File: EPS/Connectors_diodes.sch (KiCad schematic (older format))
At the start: 20 parts

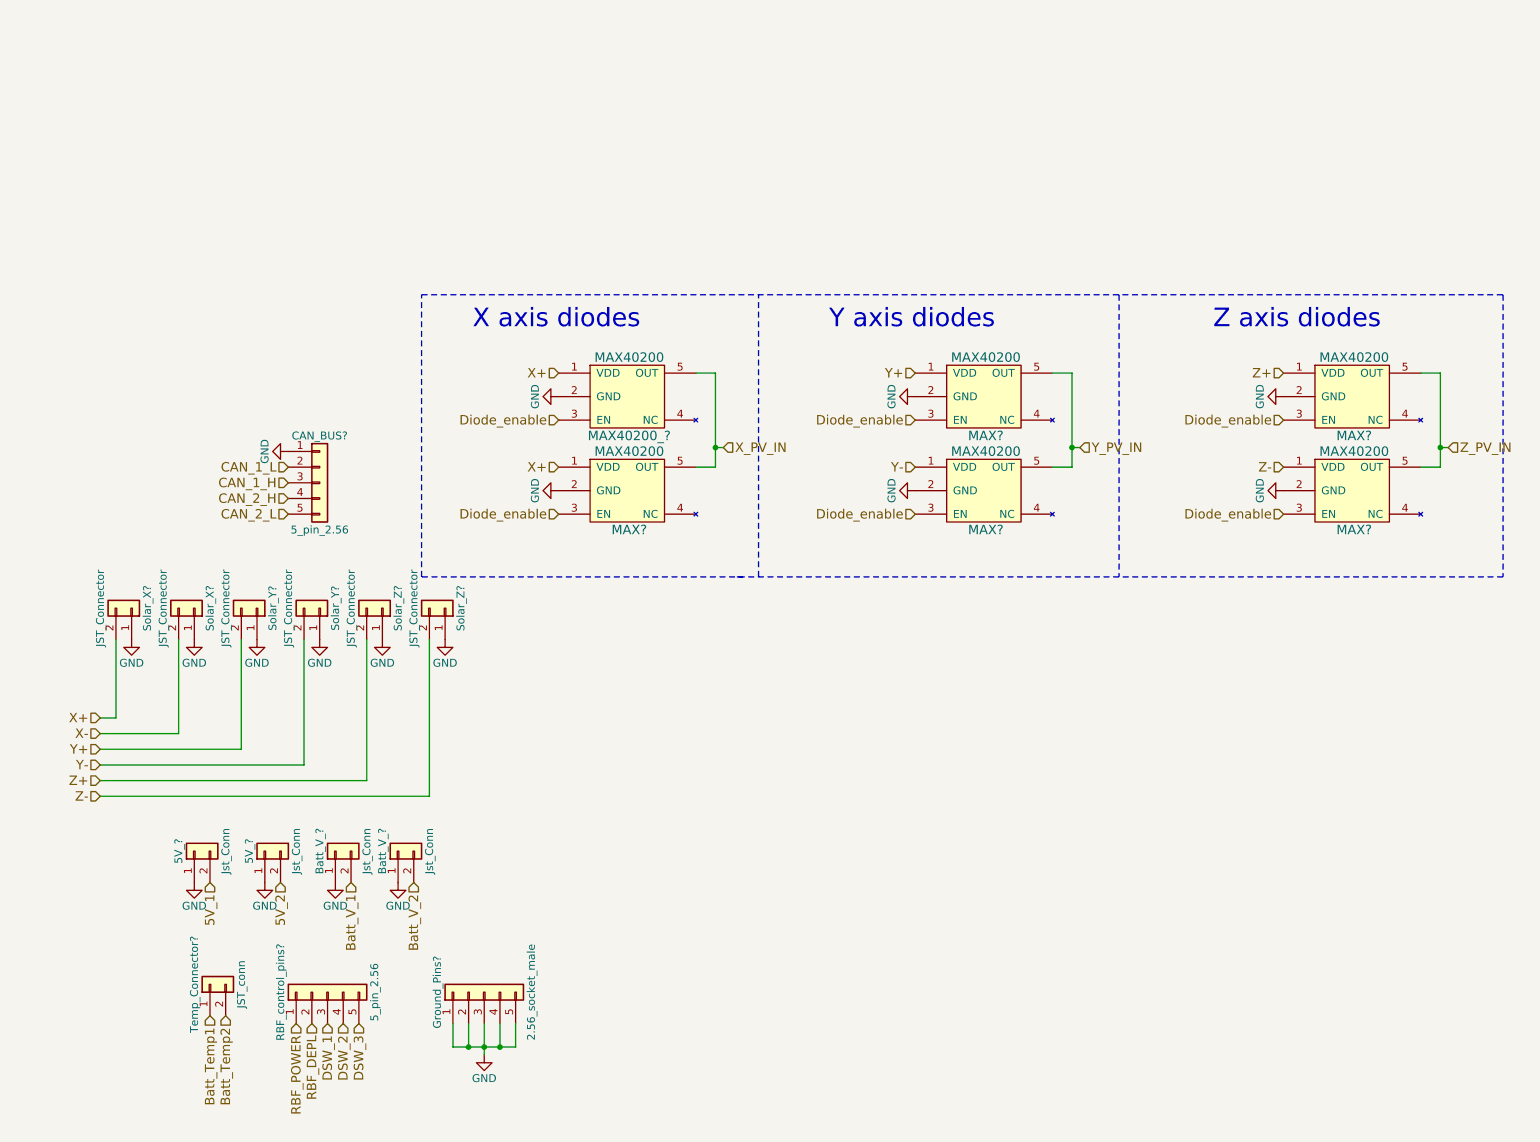
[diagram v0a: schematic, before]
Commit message: Finalized SCH (beta version) and started pcb
Capacitor banks might need to be reassigned to other locations.
No RBF pin on this SCH or PCB.
Battery gound deployment switch is fully mechanical (no mosfet switch on low side).
PCB of the prototype started. Main power converters and current measuring devices layed out.
SCH still requires ESD protection diodes!
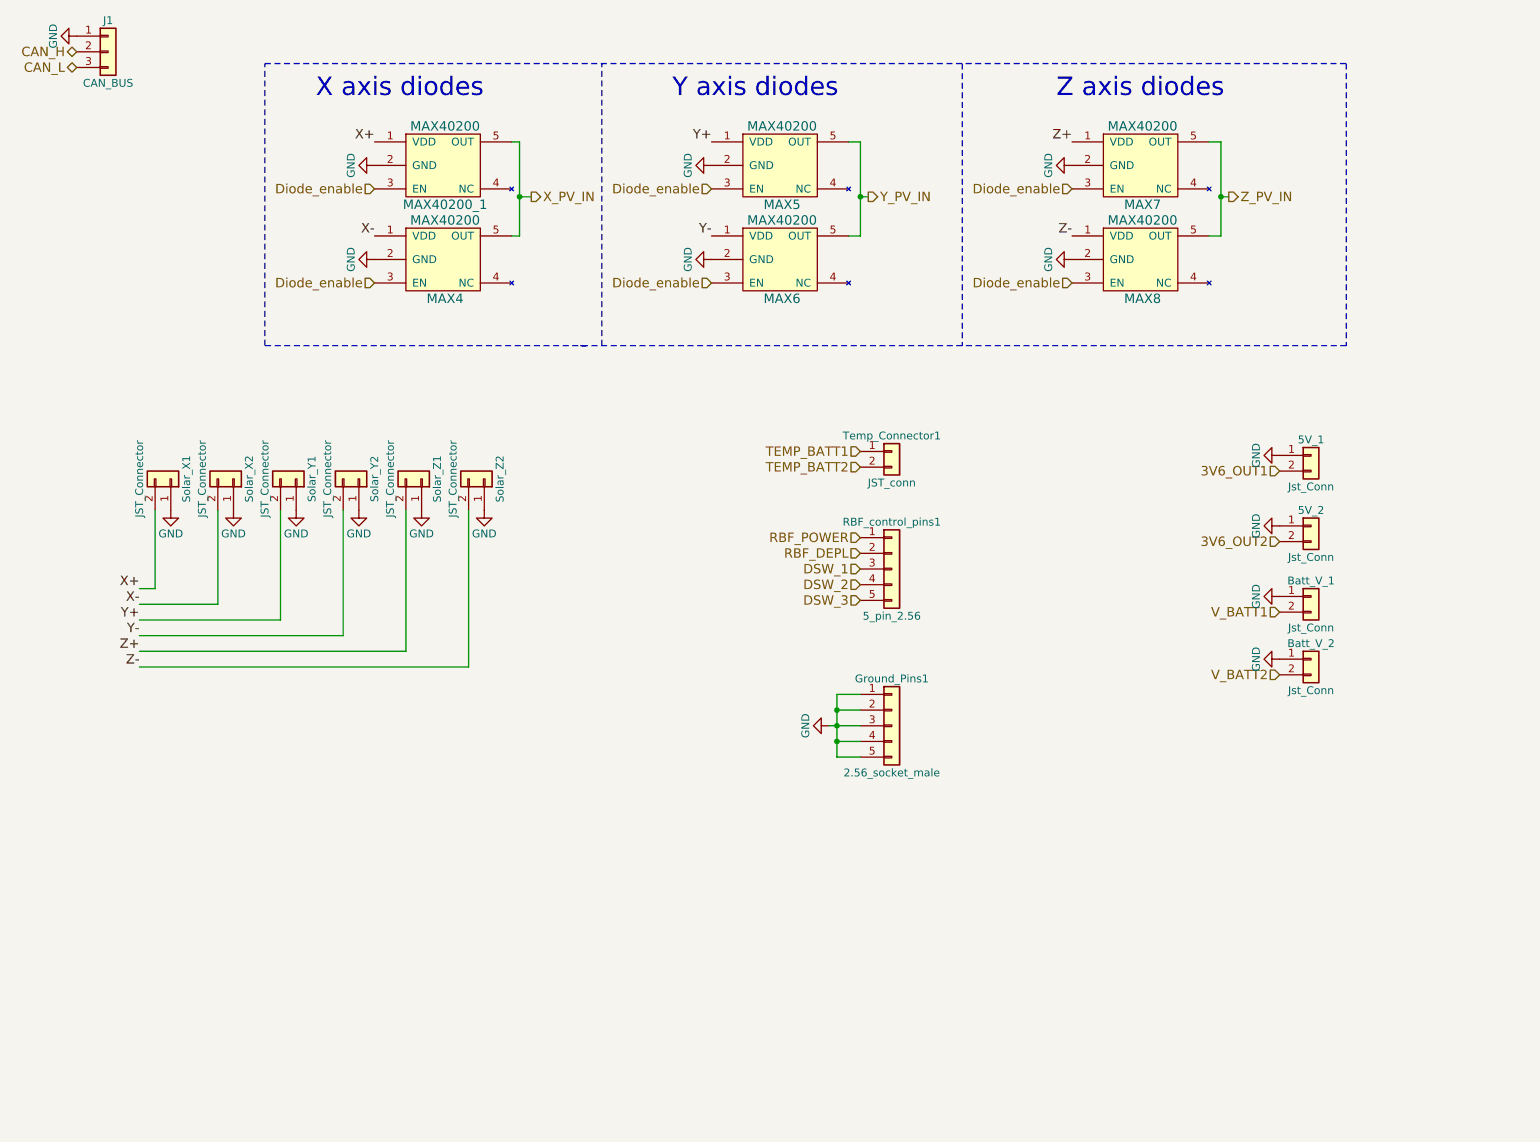
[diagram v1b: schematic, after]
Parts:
- removed CAN_BUS?: 5_pin_2.56, Socket_Strips:Socket_Strip_Straight_1x05_Pitch2.54mm, symbol Conn_01x05
- added J1: CAN_BUS, Housings_SOIC:SOIC-8_3.9x4.9mm_Pitch1.27mm, symbol Conn_01x03
- MAX4, MAX5, MAX6, MAX7, MAX8: renamed from MAX?; footprint (none) -> TO_SOT_Packages_SMD:SOT-23-5
- MAX40200_1: renamed from MAX40200_?; footprint (none) -> TO_SOT_Packages_SMD:SOT-23-5
- gave numbers to parts that had none: 13
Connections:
- net GND: now also J1.1 (Pin_1)
- net X+: no longer MAX4.1 (VDD)
- net X-: now also MAX4.1 (VDD)
- net 5V_1 renamed 3V6_OUT1
- net 5V_2 renamed 3V6_OUT2
- net Batt_Temp1 renamed TEMP_BATT1
- net Batt_Temp2 renamed TEMP_BATT2
- net Batt_V_1 renamed V_BATT1
- net Batt_V_2 renamed V_BATT2
- new net CAN_H: J1.2 (Pin_2)
- new net CAN_L: J1.3 (Pin_3)
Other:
- moved on the sheet: 5V_1, 5V_2, Batt_V_1, Batt_V_2, Ground_Pins1, MAX4, MAX40200_1, MAX5, MAX6, MAX7, MAX8, RBF_control_pins1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

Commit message: PCB updated
Added testpoints and updated PCB
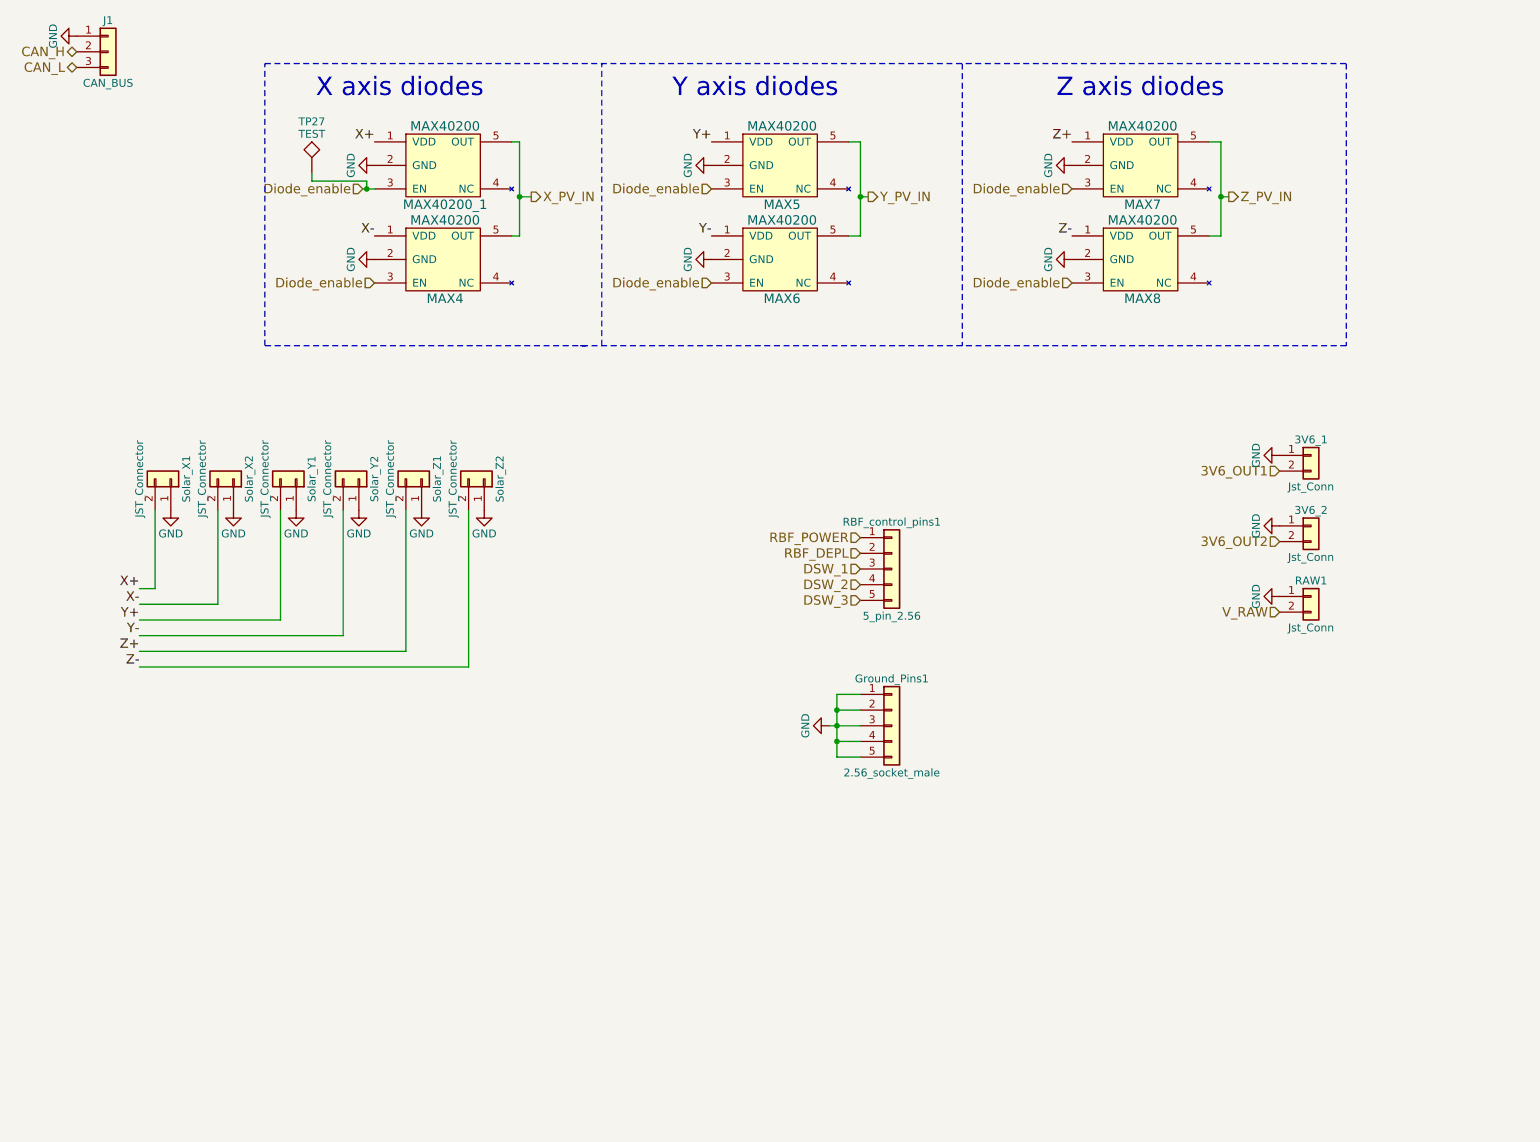
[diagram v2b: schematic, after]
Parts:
- removed Batt_V_2: Jst_Conn, Connectors_JST:JST_XH_B02B-XH-A_02x2.50mm_Straight, symbol Conn_01x02
- removed Temp_Connector1: JST_conn, Connectors_JST:JST_XH_B02B-XH-A_02x2.50mm_Straight, symbol Conn_01x02
- added TP27: TEST, Measurement_Points:Measurement_Point_Round-SMD-Pad_Small, symbol TEST
- J1: footprint Housings_SOIC:SOIC-8_3.9x4.9mm_Pitch1.27mm -> Pin_Headers:Pin_Header_Straight_1x03_Pitch2.54mm
- renumbered 5V_1 to 3V6_1, 5V_2 to 3V6_2, Batt_V_1 to RAW1
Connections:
- net Diode_enable: now also TP27.1
- net V_BATT1 renamed V_RAW
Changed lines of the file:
@@
 $EndComp
 $Comp
-L GND #PWR0135
+L GND #PWR0134
 U 1 1 5A8B7527
 P 3300 1825
-F 0 "#PWR0135" H 3300 1575 50  0001 C CNN
+F 0 "#PWR0134" H 3300 1575 50  0001 C CNN
 F 1 "GND" H 3300 1675 50  0000 C CNN
 F 2 "" H 3300 1825 50  0001 C CNN
@@
 $EndComp
 $Comp
-L GND #PWR0136
+L GND #PWR0135
 U 1 1 5A8B755E
 P 3300 2425
-F 0 "#PWR0136" H 3300 2175 50  0001 C CNN
+F 0 "#PWR0135" H 3300 2175 50  0001 C CNN
 F 1 "GND" H 3300 2275 50  0000 C CNN
 F 2 "" H 3300 2425 50  0001 C CNN
@@
 $EndComp
 $Comp
-L GND #PWR0137
+L GND #PWR0136
 U 1 1 5A8B757B
 P 5450 1825
-F 0 "#PWR0137" H 5450 1575 50  0001 C CNN
+F 0 "#PWR0136" H 5450 1575 50  0001 C CNN
 F 1 "GND" H 5450 1675 50  0000 C CNN
 F 2 "" H 5450 1825 50  0001 C CNN
@@
 $EndComp
 $Comp
-L GND #PWR0138
+L GND #PWR0137
 U 1 1 5A8B7598
 P 5450 2425
-F 0 "#PWR0138" H 5450 2175 50  0001 C CNN
+F 0 "#PWR0137" H 5450 2175 50  0001 C CNN
 F 1 "GND" H 5450 2275 50  0000 C CNN
 F 2 "" H 5450 2425 50  0001 C CNN
@@
 $EndComp
 $Comp
-L GND #PWR0139
+L GND #PWR0138
 U 1 1 5A8B75B5
 P 7750 1825
-F 0 "#PWR0139" H 7750 1575 50  0001 C CNN
+F 0 "#PWR0138" H 7750 1575 50  0001 C CNN
 F 1 "GND" H 7750 1675 50  0000 C CNN
 F 2 "" H 7750 1825 50  0001 C CNN
@@
 $EndComp
 $Comp
-L GND #PWR0140
+L GND #PWR0139
 U 1 1 5A8B75D2
 P 7750 2425
-F 0 "#PWR0140" H 7750 2175 50  0001 C CNN
+F 0 "#PWR0139" H 7750 2175 50  0001 C CNN
 F 1 "GND" H 7750 2275 50  0000 C CNN
 F 2 "" H 7750 2425 50  0001 C CNN
@@
 3V6_OUT2
 Text HLabel 9075 4675 0    60   Input ~ 0
-V_BATT1
-Text HLabel 9075 5075 0    60   Input ~ 0
-V_BATT2
+V_RAW
 Text HLabel 6400 4300 0    60   Input ~ 0
 RBF_DEPL
@@
 Wire Wire Line
 	1800 5025 3900 5025
-Text HLabel 6400 3650 0    60   Input ~ 0
-TEMP_BATT1
-Text HLabel 6400 3750 0    60   Input ~ 0
-TEMP_BATT2
 $Comp
 L Conn_01x02 Solar_X1
@@
 $EndComp
 $Comp
-L Conn_01x02 5V_2
+L Conn_01x02 3V6_2
 U 1 1 5A8D8080
 P 9275 4125
-F 0 "5V_2" H 9275 4225 50  0000 C CNN
+F 0 "3V6_2" H 9275 4225 50  0000 C CNN
 F 1 "Jst_Conn" H 9275 3925 50  0000 C CNN
 F 2 "Connectors_JST:JST_XH_B02B-XH-A_02x2.50mm_Straight" H 9275 4125 50  0001 C CNN
 F 3 "" H 9275 4125 50  0001 C CNN
 	1    9275 4125
-	1    0    0    -1
-$EndComp
-$Comp
-L Conn_01x02 Temp_Connector1
-U 1 1 5A8D8081
-P 6600 3650
-F 0 "Temp_Connector1" H 6600 3750 50  0000 C CNN
-F 1 "JST_conn" H 6600 3450 50  0000 C CNN
-F 2 "Connectors_JST:JST_XH_B02B-XH-A_02x2.50mm_Straight" H 6600 3650 50  0001 C CNN
-F 3 "" H 6600 3650 50  0001 C CNN
-	1    6600 3650
 	1    0    0    -1
 $EndComp
@@
 $EndComp
 $Comp
-L Conn_01x02 Batt_V_2
-U 1 1 5A8D8084
-P 9275 4975
-F 0 "Batt_V_2" H 9275 5075 50  0000 C CNN
-F 1 "Jst_Conn" H 9275 4775 50  0000 C CNN
-F 2 "Connectors_JST:JST_XH_B02B-XH-A_02x2.50mm_Straight" H 9275 4975 50  0001 C CNN
-F 3 "" H 9275 4975 50  0001 C CNN
-	1    9275 4975
-	1    0    0    -1
-$EndComp
-$Comp
-L Conn_01x02 Batt_V_1
+L Conn_01x02 RAW1
 U 1 1 5A8D8085
 P 9275 4575
-F 0 "Batt_V_1" H 9275 4675 50  0000 C CNN
+F 0 "RAW1" H 9275 4675 50  0000 C CNN
 F 1 "Jst_Conn" H 9275 4375 50  0000 C CNN
 F 2 "Connectors_JST:JST_XH_B02B-XH-A_02x2.50mm_Straight" H 9275 4575 50  0001 C CNN
@@
 $EndComp
 $Comp
-L GND #PWR0141
+L GND #PWR0140
 U 1 1 5A8D8086
 P 6200 5400
-F 0 "#PWR0141" H 6200 5150 50  0001 C CNN
+F 0 "#PWR0140" H 6200 5150 50  0001 C CNN
 F 1 "GND" H 6200 5250 50  0000 C CNN
 F 2 "" H 6200 5400 50  0001 C CNN
@@
 	3900 5025 3900 4025
 $Comp
-L GND #PWR0142
+L GND #PWR0141
 U 1 1 5A8D808C
 P 2000 4025
-F 0 "#PWR0142" H 2000 3775 50  0001 C CNN
+F 0 "#PWR0141" H 2000 3775 50  0001 C CNN
 F 1 "GND" H 2000 3875 50  0000 C CNN
 F 2 "" H 2000 4025 50  0001 C CNN
@@
 $EndComp
 $Comp
-L GND #PWR0143
+L GND #PWR0142
 U 1 1 5A8D808D
 P 2400 4025
-F 0 "#PWR0143" H 2400 3775 50  0001 C CNN
+F 0 "#PWR0142" H 2400 3775 50  0001 C CNN
 F 1 "GND" H 2400 3875 50  0000 C CNN
 F 2 "" H 2400 4025 50  0001 C CNN
@@
 $EndComp
 $Comp
-L GND #PWR0144
+L GND #PWR0143
 U 1 1 5A8D808E
 P 2800 4025
-F 0 "#PWR0144" H 2800 3775 50  0001 C CNN
+F 0 "#PWR0143" H 2800 3775 50  0001 C CNN
 F 1 "GND" H 2800 3875 50  0000 C CNN
 F 2 "" H 2800 4025 50  0001 C CNN
@@
 $EndComp
 $Comp
-L GND #PWR0145
+L GND #PWR0144
 U 1 1 5A8D808F
 P 3200 4025
-F 0 "#PWR0145" H 3200 3775 50  0001 C CNN
+F 0 "#PWR0144" H 3200 3775 50  0001 C CNN
 F 1 "GND" H 3200 3875 50  0000 C CNN
 F 2 "" H 3200 4025 50  0001 C CNN
@@
 $EndComp
 $Comp
-L GND #PWR0146
+L GND #PWR0145
 U 1 1 5A8D8090
 P 3600 4025
-F 0 "#PWR0146" H 3600 3775 50  0001 C CNN
+F 0 "#PWR0145" H 3600 3775 50  0001 C CNN
 F 1 "GND" H 3600 3875 50  0000 C CNN
 F 2 "" H 3600 4025 50  0001 C CNN
@@
 $EndComp
 $Comp
-L GND #PWR0147
+L GND #PWR0146
 U 1 1 5A8D8091
 P 4000 4025
-F 0 "#PWR0147" H 4000 3775 50  0001 C CNN
+F 0 "#PWR0146" H 4000 3775 50  0001 C CNN
 F 1 "GND" H 4000 3875 50  0000 C CNN
 F 2 "" H 4000 4025 50  0001 C CNN
@@
 $EndComp
 $Comp
-L Conn_01x02 5V_1
+L Conn_01x02 3V6_1
 U 1 1 5A8D8092
 P 9275 3675
-F 0 "5V_1" H 9275 3775 50  0000 C CNN
+F 0 "3V6_1" H 9275 3775 50  0000 C CNN
 F 1 "Jst_Conn" H 9275 3475 50  0000 C CNN
 F 2 "Connectors_JST:JST_XH_B02B-XH-A_02x2.50mm_Straight" H 9275 3675 50  0001 C CNN
@@
 $EndComp
 $Comp
-L GND #PWR0148
+L GND #PWR0147
 U 1 1 5A8D8093
 P 9075 3675
-F 0 "#PWR0148" H 9075 3425 50  0001 C CNN
+F 0 "#PWR0147" H 9075 3425 50  0001 C CNN
 F 1 "GND" H 9075 3525 50  0000 C CNN
 F 2 "" H 9075 3675 50  0001 C CNN
@@
 $EndComp
 $Comp
-L GND #PWR0149
+L GND #PWR0148
 U 1 1 5A8D8094
 P 9075 4125
-F 0 "#PWR0149" H 9075 3875 50  0001 C CNN
+F 0 "#PWR0148" H 9075 3875 50  0001 C CNN
 F 1 "GND" H 9075 3975 50  0000 C CNN
 F 2 "" H 9075 4125 50  0001 C CNN
@@
 $EndComp
 $Comp
-L GND #PWR0150
+L GND #PWR0149
 U 1 1 5A8D8095
 P 9075 4575
-F 0 "#PWR0150" H 9075 4325 50  0001 C CNN
+F 0 "#PWR0149" H 9075 4325 50  0001 C CNN
 F 1 "GND" H 9075 4425 50  0000 C CNN
 F 2 "" H 9075 4575 50  0001 C CNN
@@
 	0    1    1    0
 $EndComp
-$Comp
-L GND #PWR0151
-U 1 1 5A8D8096
-P 9075 4975
-F 0 "#PWR0151" H 9075 4725 50  0001 C CNN
-F 1 "GND" H 9075 4825 50  0000 C CNN
-F 2 "" H 9075 4975 50  0001 C CNN
-F 3 "" H 9075 4975 50  0001 C CNN
-	1    9075 4975
-	0    1    1    0
-$EndComp
-Text HLabel 3300 1975 0    60   Input ~ 0
+Text HLabel 3225 1975 0    60   Input ~ 0
 Diode_enable
 Text HLabel 3300 2575 0    60   Input ~ 0
@@
 F 0 "J1" H 1600 1300 50  0000 C CNN
 F 1 "CAN_BUS" H 1600 900 50  0000 C CNN
-F 2 "Housings_SOIC:SOIC-8_3.9x4.9mm_Pitch1.27mm" H 1600 1100 50  0001 C CNN
+F 2 "Pin_Headers:Pin_Header_Straight_1x03_Pitch2.54mm" H 1600 1100 50  0001 C CNN
 F 3 "" H 1600 1100 50  0001 C CNN
 	1    1600 1100
@@
 CAN_L
 $Comp
-L GND #PWR0152
+L GND #PWR0150
 U 1 1 5A8EF3B3
 P 1400 1000
-F 0 "#PWR0152" H 1400 750 50  0001 C CNN
+F 0 "#PWR0150" H 1400 750 50  0001 C CNN
 F 1 "GND" H 1400 850 50  0000 C CNN
 F 2 "" H 1400 1000 50  0001 C CNN
@@
 	8700 2275 8625 2275
 Connection ~ 8700 2025
+$Comp
+L TEST TP27
+U 1 1 5A9F37AF
+P 2900 1875
+F 0 "TP27" H 2900 2175 50  0000 C BNN
+F 1 "TEST" H 2900 2125 50  0000 C CNN
+F 2 "Measurement_Points:Measurement_Point_Round-SMD-Pad_Small" H 2900 1875 50  0001 C CNN
+F 3 "" H 2900 1875 50  0001 C CNN
+	1    2900 1875
+	1    0    0    -1
+$EndComp
+Wire Wire Line
+	3225 1975 3300 1975
+Wire Wire Line
+	3250 1975 3250 1925
+Wire Wire Line
+	3250 1925 2900 1925
+Wire Wire Line
+	2900 1925 2900 1875
+Connection ~ 3250 1975
 $EndSCHEMATC
